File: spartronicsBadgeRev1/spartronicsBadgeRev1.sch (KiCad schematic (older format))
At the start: 54 parts, among them U1 ATmega328PB-AU

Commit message: Checkpoint before doing routing, in case of error
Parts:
- J_Debug1: footprint Connector_PinSocket_2.54mm:PinSocket_2x03_P2.54mm_Horizontal -> Connector_PinHeader_2.54mm:PinHeader_2x03_P2.54mm_Vertical
- J_ExtPwr1: footprint Connector_PinSocket_2.54mm:PinSocket_1x02_P2.54mm_Horizontal -> Connector_PinHeader_2.54mm:PinHeader_1x02_P2.54mm_Vertical
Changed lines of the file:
@@
 EESchema Schematic File Version 4
 LIBS:spartronicsBadgeRev1-cache
-EELAYER 26 0
+EELAYER 30 0
 EELAYER END
 $Descr A4 11693 8268
@@
 F 0 "J_ExtPwr1" V 4650 1100 50  0000 L CNN
 F 1 "Conn_01x02" V 4750 850 50  0000 L CNN
-F 2 "Connector_PinSocket_2.54mm:PinSocket_1x02_P2.54mm_Horizontal" H 4650 1000 50  0001 C CNN
+F 2 "Connector_PinHeader_2.54mm:PinHeader_1x02_P2.54mm_Vertical" H 4650 1000 50  0001 C CNN
 F 3 "~" H 4650 1000 50  0001 C CNN
 	1    4650 1000
@@
 F 0 "J_Debug1" H 4700 3467 50  0000 C CNN
 F 1 "Conn_02x03" H 4700 3376 50  0000 C CNN
-F 2 "Connector_PinSocket_2.54mm:PinSocket_2x03_P2.54mm_Horizontal" H 4650 3150 50  0001 C CNN
+F 2 "Connector_PinHeader_2.54mm:PinHeader_2x03_P2.54mm_Vertical" H 4650 3150 50  0001 C CNN
 F 3 "~" H 4650 3150 50  0001 C CNN
 	1    4650 3150

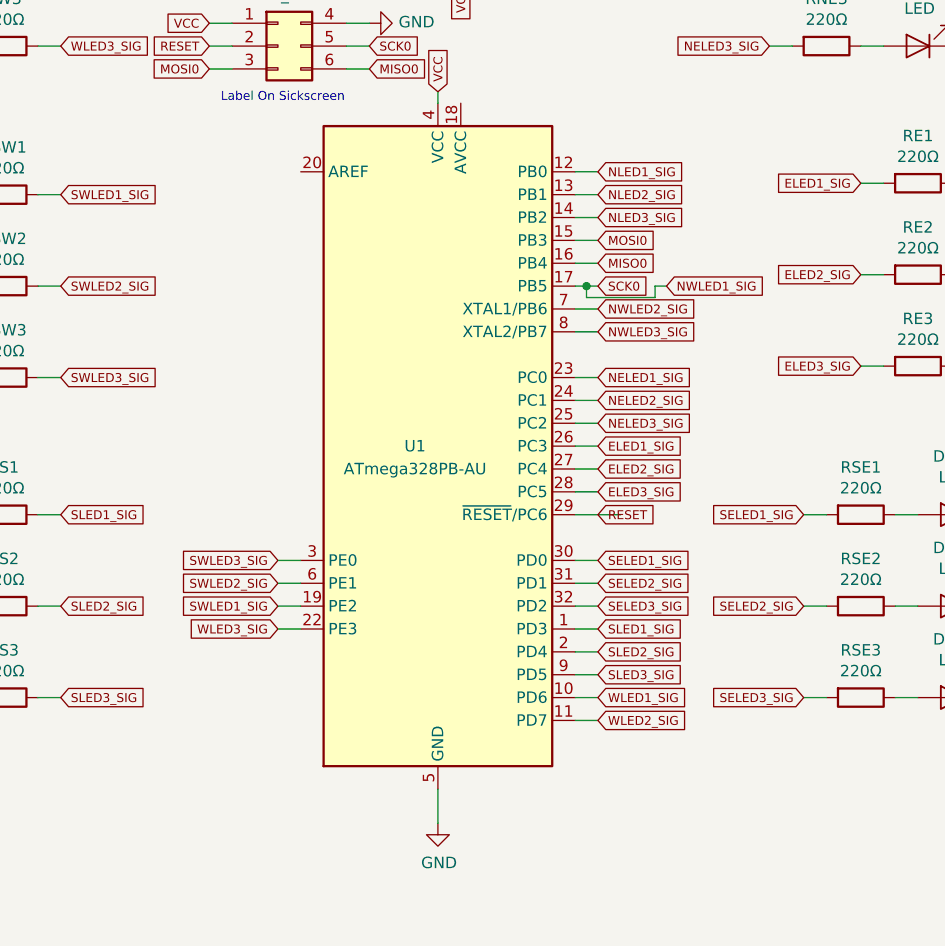
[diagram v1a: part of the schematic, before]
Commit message: Finished routing, labels on back, added ground plane. Almost ready for build
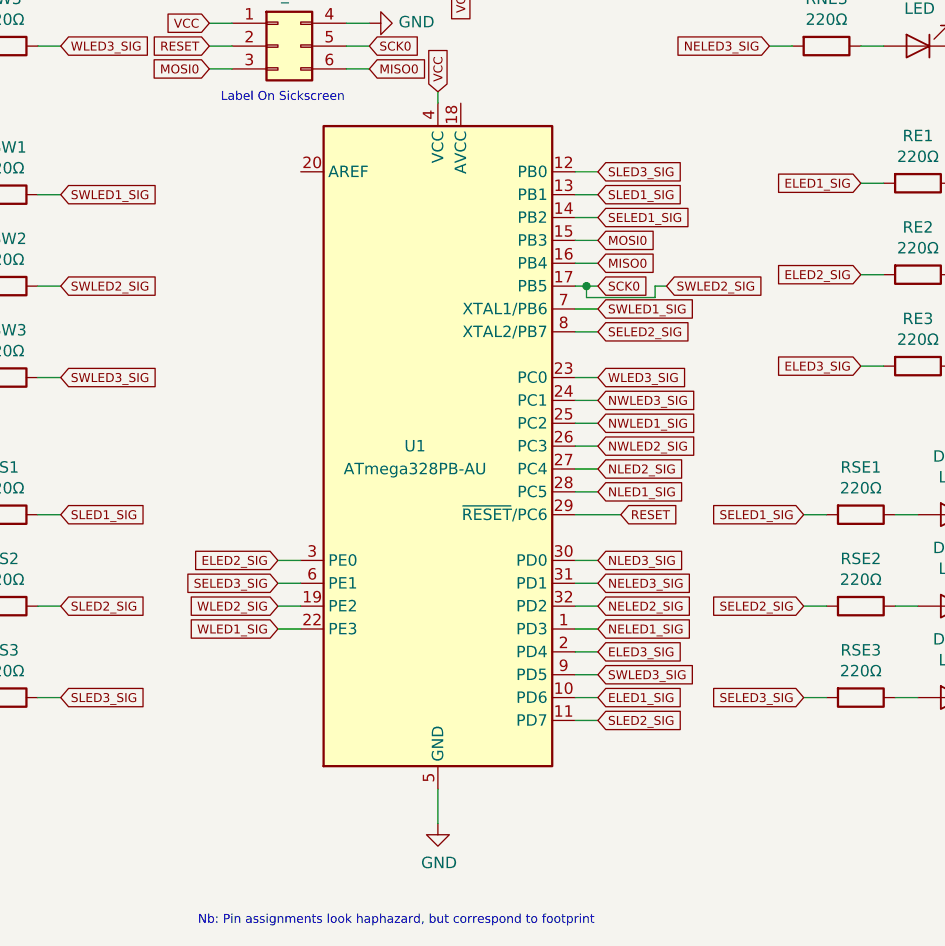
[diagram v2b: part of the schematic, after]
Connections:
- net ELED1_SIG: now also U1.10 (PD6); no longer U1.26 (PC3)
- net ELED2_SIG: now also U1.3 (PE0); no longer U1.27 (PC4)
- net ELED3_SIG: now also U1.2 (PD4); no longer U1.28 (PC5)
- net NELED1_SIG: now also U1.1 (PD3); no longer U1.23 (PC0)
- net NELED2_SIG: now also U1.32 (PD2); no longer U1.24 (PC1)
- net NELED3_SIG: now also U1.31 (PD1); no longer U1.25 (PC2)
- net NLED1_SIG: now also U1.28 (PC5); no longer U1.12 (PB0)
- net NLED2_SIG: now also U1.27 (PC4); no longer U1.13 (PB1)
- net NLED3_SIG: now also U1.30 (PD0); no longer U1.14 (PB2)
- net NWLED1_SIG: now also U1.25 (PC2); no longer J_Debug1.5 (Pin_5), U1.17 (PB5)
- net NWLED2_SIG: now also U1.26 (PC3); no longer U1.7 (XTAL1/PB6)
- net NWLED3_SIG: now also U1.24 (PC1); no longer U1.8 (XTAL2/PB7)
- net SELED1_SIG: now also U1.14 (PB2); no longer U1.30 (PD0)
- net SELED2_SIG: now also U1.8 (XTAL2/PB7); no longer U1.31 (PD1)
- net SELED3_SIG: now also U1.6 (PE1); no longer U1.32 (PD2)
- net SLED1_SIG: now also U1.13 (PB1); no longer U1.1 (PD3)
- net SLED2_SIG: now also U1.11 (PD7); no longer U1.2 (PD4)
- net SLED3_SIG: now also U1.12 (PB0); no longer U1.9 (PD5)
- net SWLED1_SIG: now also U1.7 (XTAL1/PB6); no longer U1.19 (PE2)
- net SWLED3_SIG: now also U1.9 (PD5); no longer U1.3 (PE0)
- net WLED1_SIG: now also U1.22 (PE3); no longer U1.10 (PD6)
- net WLED2_SIG: now also U1.19 (PE2); no longer U1.11 (PD7)
- net WLED3_SIG: now also U1.23 (PC0); no longer U1.22 (PE3)
- net SWLED2_SIG renamed SCK0
- net SCK0: now also J_Debug1.5 (Pin_5), U1.17 (PB5); no longer U1.6 (PE1)
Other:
- note added: "Nb: Pin assignments look haphazard, but correspond to footprint\n"
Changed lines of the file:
@@
 	1    0    0    -1
 $EndComp
-Text GLabel 6050 5200 2    39   Input ~ 0
+Text GLabel 6150 5200 2    39   Input ~ 0
 RESET
 Wire Wire Line
@@
 Text Notes 4100 1850 0    39   ~ 0
 Later Revisions add reverse \nprotection(shotkeyy) diode here?
+Text GLabel 6050 5100 2    39   Input ~ 0
+NLED1_SIG
+Text GLabel 6050 5000 2    39   Input ~ 0
+NLED2_SIG
+Text GLabel 6050 5400 2    39   Input ~ 0
+NLED3_SIG
+Wire Wire Line
+	5950 3700 6050 3700
+Wire Wire Line
+	5950 3800 6050 3800
+Wire Wire Line
+	5950 3900 6050 3900
+Text GLabel 6050 5700 2    39   Input ~ 0
+NELED1_SIG
+Text GLabel 6050 5600 2    39   Input ~ 0
+NELED2_SIG
+Text GLabel 6050 5500 2    39   Input ~ 0
+NELED3_SIG
+Text GLabel 6050 6000 2    39   Input ~ 0
+ELED1_SIG
+Text GLabel 4650 5400 0    39   Input ~ 0
+ELED2_SIG
+Text GLabel 6050 5800 2    39   Input ~ 0
+ELED3_SIG
+Text GLabel 6050 3900 2    39   Input ~ 0
+SELED1_SIG
+Text GLabel 6050 4400 2    39   Input ~ 0
+SELED2_SIG
+Text GLabel 4650 5500 0    39   Input ~ 0
+SELED3_SIG
+Text GLabel 6050 3800 2    39   Input ~ 0
+SLED1_SIG
+Text GLabel 6050 6100 2    39   Input ~ 0
+SLED2_SIG
 Text GLabel 6050 3700 2    39   Input ~ 0
-NLED1_SIG
-Text GLabel 6050 3800 2    39   Input ~ 0
-NLED2_SIG
-Text GLabel 6050 3900 2    39   Input ~ 0
-NLED3_SIG
-Wire Wire Line
-	5950 3700 6050 3700
-Wire Wire Line
-	5950 3800 6050 3800
-Wire Wire Line
-	5950 3900 6050 3900
-Text GLabel 6050 4600 2    39   Input ~ 0
-NELED1_SIG
-Text GLabel 6050 4700 2    39   Input ~ 0
-NELED2_SIG
-Text GLabel 6050 4800 2    39   Input ~ 0
-NELED3_SIG
-Text GLabel 6050 4900 2    39   Input ~ 0
-ELED1_SIG
-Text GLabel 6050 5000 2    39   Input ~ 0
-ELED2_SIG
-Text GLabel 6050 5100 2    39   Input ~ 0
-ELED3_SIG
-Text GLabel 6050 5400 2    39   Input ~ 0
-SELED1_SIG
-Text GLabel 6050 5500 2    39   Input ~ 0
-SELED2_SIG
-Text GLabel 6050 5600 2    39   Input ~ 0
-SELED3_SIG
-Text GLabel 6050 5700 2    39   Input ~ 0
-SLED1_SIG
-Text GLabel 6050 5800 2    39   Input ~ 0
-SLED2_SIG
+SLED3_SIG
+Text GLabel 6050 4300 2    39   Input ~ 0
+SWLED1_SIG
+Text GLabel 6350 4200 2    39   Input ~ 0
+SWLED2_SIG
 Text GLabel 6050 5900 2    39   Input ~ 0
-SLED3_SIG
-Text GLabel 4650 5600 0    39   Input ~ 0
-SWLED1_SIG
-Text GLabel 4650 5500 0    39   Input ~ 0
-SWLED2_SIG
-Text GLabel 4650 5400 0    39   Input ~ 0
 SWLED3_SIG
 $Comp
@@
 	0    1    1    0
 $EndComp
-Text GLabel 6050 6000 2    39   Input ~ 0
+Text GLabel 4650 5700 0    39   Input ~ 0
 WLED1_SIG
-Text GLabel 6050 6100 2    39   Input ~ 0
+Text GLabel 4650 5600 0    39   Input ~ 0
 WLED2_SIG
-Text GLabel 4650 5700 0    39   Input ~ 0
+Text GLabel 6050 4600 2    39   Input ~ 0
 WLED3_SIG
 Wire Wire Line
@@
 Wire Wire Line
 	6050 4600 5950 4600
-Text GLabel 6350 4200 2    39   Input ~ 0
+Text GLabel 6050 4800 2    39   Input ~ 0
 NWLED1_SIG
-Text GLabel 6050 4300 2    39   Input ~ 0
+Text GLabel 6050 4900 2    39   Input ~ 0
 NWLED2_SIG
-Text GLabel 6050 4400 2    39   Input ~ 0
+Text GLabel 6050 4700 2    39   Input ~ 0
 NWLED3_SIG
 Wire Wire Line
@@
 Wire Wire Line
 	5150 1000 5050 1000
+Text Notes 4300 7000 0    39   ~ 0
+Nb: Pin assignments look haphazard, but correspond to footprint\n
 $EndSCHEMATC

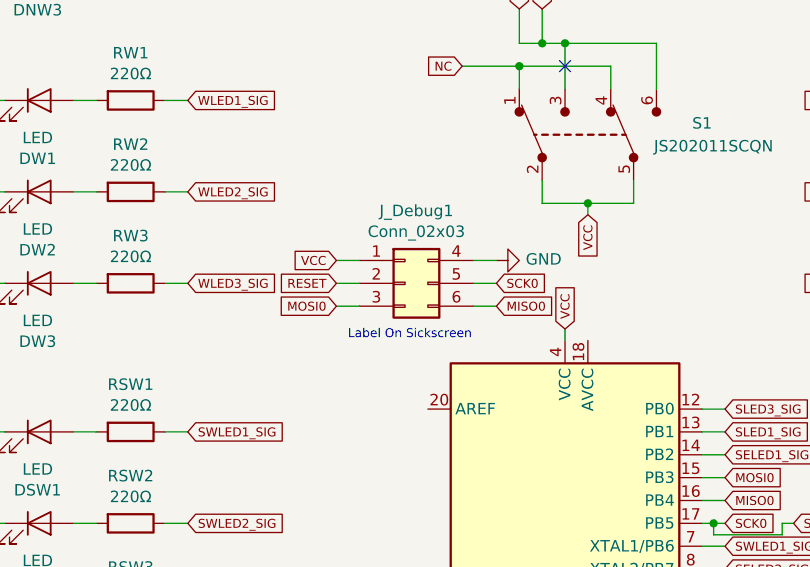
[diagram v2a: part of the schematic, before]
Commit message: :dizzy: Re-assigning footprint to Diodes + Debug connector (Had to re-assign some pins) (Full 3D render now!)
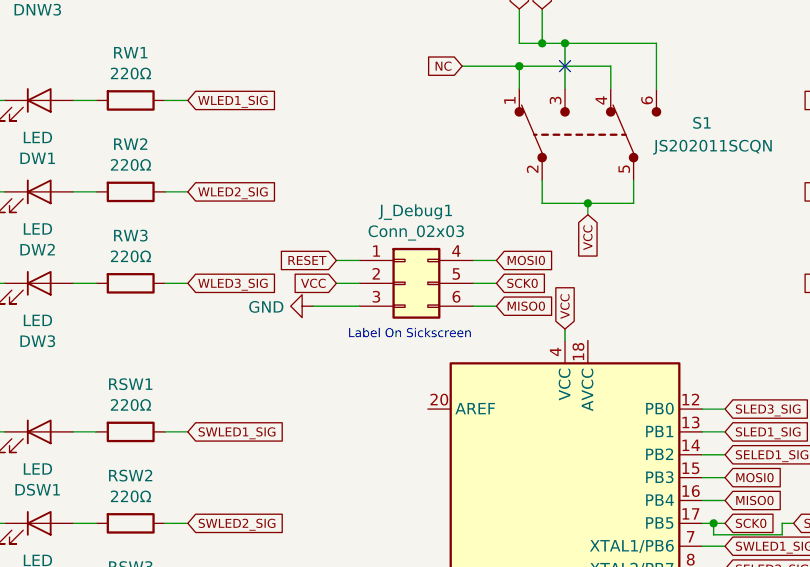
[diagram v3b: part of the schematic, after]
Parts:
- DE1, DE2, DE3, DN1, DN2, DN3, DNE1, DNE2, DNE3, DNW1, DNW2, DNW3, DS1, DS2, DS3, DSE1, DSE2, DSE3, DSW1, DSW2, DSW3, DW1, DW2, DW3: footprint Diode_SMD:D_0603_1608Metric_Pad1.05x0.95mm_HandSolder -> LED_SMD:LED_0603_1608Metric_Pad1.05x0.95mm_HandSolder
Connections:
- net GND: now also J_Debug1.3 (Pin_3); no longer J_Debug1.4 (Pin_4)
- net MOSI0: now also J_Debug1.4 (Pin_4); no longer J_Debug1.3 (Pin_3)
- net RESET: now also J_Debug1.1 (Pin_1); no longer J_Debug1.2 (Pin_2)
- net VCC: now also J_Debug1.2 (Pin_2); no longer J_Debug1.1 (Pin_1)
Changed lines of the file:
@@
 F 0 "DN1" H 7643 645 50  0000 C CNN
 F 1 "LED" H 7643 736 50  0000 C CNN
-F 2 "Diode_SMD:D_0603_1608Metric_Pad1.05x0.95mm_HandSolder" H 7650 900 50  0001 C CNN
+F 2 "LED_SMD:LED_0603_1608Metric_Pad1.05x0.95mm_HandSolder" H 7650 900 50  0001 C CNN
 F 3 "~" H 7650 900 50  0001 C CNN
 	1    7650 900
@@
 F 0 "DN2" H 7643 1045 50  0000 C CNN
 F 1 "LED" H 7643 1136 50  0000 C CNN
-F 2 "Diode_SMD:D_0603_1608Metric_Pad1.05x0.95mm_HandSolder" H 7650 1300 50  0001 C CNN
+F 2 "LED_SMD:LED_0603_1608Metric_Pad1.05x0.95mm_HandSolder" H 7650 1300 50  0001 C CNN
 F 3 "~" H 7650 1300 50  0001 C CNN
 	1    7650 1300
@@
 F 0 "DN3" H 7643 1445 50  0000 C CNN
 F 1 "LED" H 7643 1536 50  0000 C CNN
-F 2 "Diode_SMD:D_0603_1608Metric_Pad1.05x0.95mm_HandSolder" H 7650 1700 50  0001 C CNN
+F 2 "LED_SMD:LED_0603_1608Metric_Pad1.05x0.95mm_HandSolder" H 7650 1700 50  0001 C CNN
 F 3 "~" H 7650 1700 50  0001 C CNN
 	1    7650 1700
@@
 F 0 "DNE1" H 7443 2095 50  0000 C CNN
 F 1 "LED" H 7443 2186 50  0000 C CNN
-F 2 "Diode_SMD:D_0603_1608Metric_Pad1.05x0.95mm_HandSolder" H 7450 2350 50  0001 C CNN
+F 2 "LED_SMD:LED_0603_1608Metric_Pad1.05x0.95mm_HandSolder" H 7450 2350 50  0001 C CNN
 F 3 "~" H 7450 2350 50  0001 C CNN
 	1    7450 2350
@@
 F 0 "DNE2" H 7443 2495 50  0000 C CNN
 F 1 "LED" H 7443 2586 50  0000 C CNN
-F 2 "Diode_SMD:D_0603_1608Metric_Pad1.05x0.95mm_HandSolder" H 7450 2750 50  0001 C CNN
+F 2 "LED_SMD:LED_0603_1608Metric_Pad1.05x0.95mm_HandSolder" H 7450 2750 50  0001 C CNN
 F 3 "~" H 7450 2750 50  0001 C CNN
 	1    7450 2750
@@
 F 0 "DNE3" H 7443 2895 50  0000 C CNN
 F 1 "LED" H 7443 2986 50  0000 C CNN
-F 2 "Diode_SMD:D_0603_1608Metric_Pad1.05x0.95mm_HandSolder" H 7450 3150 50  0001 C CNN
+F 2 "LED_SMD:LED_0603_1608Metric_Pad1.05x0.95mm_HandSolder" H 7450 3150 50  0001 C CNN
 F 3 "~" H 7450 3150 50  0001 C CNN
 	1    7450 3150
@@
 F 0 "DE1" H 7843 3495 50  0000 C CNN
 F 1 "LED" H 7843 3586 50  0000 C CNN
-F 2 "Diode_SMD:D_0603_1608Metric_Pad1.05x0.95mm_HandSolder" H 7850 3750 50  0001 C CNN
+F 2 "LED_SMD:LED_0603_1608Metric_Pad1.05x0.95mm_HandSolder" H 7850 3750 50  0001 C CNN
 F 3 "~" H 7850 3750 50  0001 C CNN
 	1    7850 3750
@@
 F 0 "DE2" H 7843 3895 50  0000 C CNN
 F 1 "LED" H 7843 3986 50  0000 C CNN
-F 2 "Diode_SMD:D_0603_1608Metric_Pad1.05x0.95mm_HandSolder" H 7850 4150 50  0001 C CNN
+F 2 "LED_SMD:LED_0603_1608Metric_Pad1.05x0.95mm_HandSolder" H 7850 4150 50  0001 C CNN
 F 3 "~" H 7850 4150 50  0001 C CNN
 	1    7850 4150
@@
 F 0 "DE3" H 7843 4295 50  0000 C CNN
 F 1 "LED" H 7843 4386 50  0000 C CNN
-F 2 "Diode_SMD:D_0603_1608Metric_Pad1.05x0.95mm_HandSolder" H 7850 4550 50  0001 C CNN
+F 2 "LED_SMD:LED_0603_1608Metric_Pad1.05x0.95mm_HandSolder" H 7850 4550 50  0001 C CNN
 F 3 "~" H 7850 4550 50  0001 C CNN
 	1    7850 4550
@@
 F 0 "DSE1" H 7593 4945 50  0000 C CNN
 F 1 "LED" H 7593 5036 50  0000 C CNN
-F 2 "Diode_SMD:D_0603_1608Metric_Pad1.05x0.95mm_HandSolder" H 7600 5200 50  0001 C CNN
+F 2 "LED_SMD:LED_0603_1608Metric_Pad1.05x0.95mm_HandSolder" H 7600 5200 50  0001 C CNN
 F 3 "~" H 7600 5200 50  0001 C CNN
 	1    7600 5200
@@
 F 0 "DSE2" H 7593 5345 50  0000 C CNN
 F 1 "LED" H 7593 5436 50  0000 C CNN
-F 2 "Diode_SMD:D_0603_1608Metric_Pad1.05x0.95mm_HandSolder" H 7600 5600 50  0001 C CNN
+F 2 "LED_SMD:LED_0603_1608Metric_Pad1.05x0.95mm_HandSolder" H 7600 5600 50  0001 C CNN
 F 3 "~" H 7600 5600 50  0001 C CNN
 	1    7600 5600
@@
 F 0 "DSE3" H 7593 5745 50  0000 C CNN
 F 1 "LED" H 7593 5836 50  0000 C CNN
-F 2 "Diode_SMD:D_0603_1608Metric_Pad1.05x0.95mm_HandSolder" H 7600 6000 50  0001 C CNN
+F 2 "LED_SMD:LED_0603_1608Metric_Pad1.05x0.95mm_HandSolder" H 7600 6000 50  0001 C CNN
 F 3 "~" H 7600 6000 50  0001 C CNN
 	1    7600 6000
@@
 F 0 "DNW3" H 3043 1445 50  0000 C CNN
 F 1 "LED" H 3043 1536 50  0000 C CNN
-F 2 "Diode_SMD:D_0603_1608Metric_Pad1.05x0.95mm_HandSolder" H 3050 1700 50  0001 C CNN
+F 2 "LED_SMD:LED_0603_1608Metric_Pad1.05x0.95mm_HandSolder" H 3050 1700 50  0001 C CNN
 F 3 "~" H 3050 1700 50  0001 C CNN
 	1    3050 1700
@@
 F 0 "DNW2" H 3043 1045 50  0000 C CNN
 F 1 "LED" H 3043 1136 50  0000 C CNN
-F 2 "Diode_SMD:D_0603_1608Metric_Pad1.05x0.95mm_HandSolder" H 3050 1300 50  0001 C CNN
+F 2 "LED_SMD:LED_0603_1608Metric_Pad1.05x0.95mm_HandSolder" H 3050 1300 50  0001 C CNN
 F 3 "~" H 3050 1300 50  0001 C CNN
 	1    3050 1300
@@
 F 0 "DNW1" H 3043 645 50  0000 C CNN
 F 1 "LED" H 3043 736 50  0000 C CNN
-F 2 "Diode_SMD:D_0603_1608Metric_Pad1.05x0.95mm_HandSolder" H 3050 900 50  0001 C CNN
+F 2 "LED_SMD:LED_0603_1608Metric_Pad1.05x0.95mm_HandSolder" H 3050 900 50  0001 C CNN
 F 3 "~" H 3050 900 50  0001 C CNN
 	1    3050 900
@@
 F 0 "DW3" H 3043 2895 50  0000 C CNN
 F 1 "LED" H 3043 2986 50  0000 C CNN
-F 2 "Diode_SMD:D_0603_1608Metric_Pad1.05x0.95mm_HandSolder" H 3050 3150 50  0001 C CNN
+F 2 "LED_SMD:LED_0603_1608Metric_Pad1.05x0.95mm_HandSolder" H 3050 3150 50  0001 C CNN
 F 3 "~" H 3050 3150 50  0001 C CNN
 	1    3050 3150
@@
 F 0 "DW2" H 3043 2495 50  0000 C CNN
 F 1 "LED" H 3043 2586 50  0000 C CNN
-F 2 "Diode_SMD:D_0603_1608Metric_Pad1.05x0.95mm_HandSolder" H 3050 2750 50  0001 C CNN
+F 2 "LED_SMD:LED_0603_1608Metric_Pad1.05x0.95mm_HandSolder" H 3050 2750 50  0001 C CNN
 F 3 "~" H 3050 2750 50  0001 C CNN
 	1    3050 2750
@@
 F 0 "DW1" H 3043 2095 50  0000 C CNN
 F 1 "LED" H 3043 2186 50  0000 C CNN
-F 2 "Diode_SMD:D_0603_1608Metric_Pad1.05x0.95mm_HandSolder" H 3050 2350 50  0001 C CNN
+F 2 "LED_SMD:LED_0603_1608Metric_Pad1.05x0.95mm_HandSolder" H 3050 2350 50  0001 C CNN
 F 3 "~" H 3050 2350 50  0001 C CNN
 	1    3050 2350
@@
 F 0 "DSW3" H 3043 4345 50  0000 C CNN
 F 1 "LED" H 3043 4436 50  0000 C CNN
-F 2 "Diode_SMD:D_0603_1608Metric_Pad1.05x0.95mm_HandSolder" H 3050 4600 50  0001 C CNN
+F 2 "LED_SMD:LED_0603_1608Metric_Pad1.05x0.95mm_HandSolder" H 3050 4600 50  0001 C CNN
 F 3 "~" H 3050 4600 50  0001 C CNN
 	1    3050 4600
@@
 F 0 "DSW2" H 3043 3945 50  0000 C CNN
 F 1 "LED" H 3043 4036 50  0000 C CNN
-F 2 "Diode_SMD:D_0603_1608Metric_Pad1.05x0.95mm_HandSolder" H 3050 4200 50  0001 C CNN
+F 2 "LED_SMD:LED_0603_1608Metric_Pad1.05x0.95mm_HandSolder" H 3050 4200 50  0001 C CNN
 F 3 "~" H 3050 4200 50  0001 C CNN
 	1    3050 4200
@@
 F 0 "DSW1" H 3043 3545 50  0000 C CNN
 F 1 "LED" H 3043 3636 50  0000 C CNN
-F 2 "Diode_SMD:D_0603_1608Metric_Pad1.05x0.95mm_HandSolder" H 3050 3800 50  0001 C CNN
+F 2 "LED_SMD:LED_0603_1608Metric_Pad1.05x0.95mm_HandSolder" H 3050 3800 50  0001 C CNN
 F 3 "~" H 3050 3800 50  0001 C CNN
 	1    3050 3800
@@
 F 0 "DS3" H 3043 5745 50  0000 C CNN
 F 1 "LED" H 3043 5836 50  0000 C CNN
-F 2 "Diode_SMD:D_0603_1608Metric_Pad1.05x0.95mm_HandSolder" H 3050 6000 50  0001 C CNN
+F 2 "LED_SMD:LED_0603_1608Metric_Pad1.05x0.95mm_HandSolder" H 3050 6000 50  0001 C CNN
 F 3 "~" H 3050 6000 50  0001 C CNN
 	1    3050 6000
@@
 F 0 "DS2" H 3043 5345 50  0000 C CNN
 F 1 "LED" H 3043 5436 50  0000 C CNN
-F 2 "Diode_SMD:D_0603_1608Metric_Pad1.05x0.95mm_HandSolder" H 3050 5600 50  0001 C CNN
+F 2 "LED_SMD:LED_0603_1608Metric_Pad1.05x0.95mm_HandSolder" H 3050 5600 50  0001 C CNN
 F 3 "~" H 3050 5600 50  0001 C CNN
 	1    3050 5600
@@
 F 0 "DS1" H 3043 4945 50  0000 C CNN
 F 1 "LED" H 3043 5036 50  0000 C CNN
-F 2 "Diode_SMD:D_0603_1608Metric_Pad1.05x0.95mm_HandSolder" H 3050 5200 50  0001 C CNN
+F 2 "LED_SMD:LED_0603_1608Metric_Pad1.05x0.95mm_HandSolder" H 3050 5200 50  0001 C CNN
 F 3 "~" H 3050 5200 50  0001 C CNN
 	1    3050 5200
@@
 Wire Wire Line
 	5950 5200 6150 5200
-Text GLabel 4350 3150 0    39   Input ~ 0
+Text GLabel 4350 3050 0    39   Input ~ 0
 RESET
 Wire Wire Line
@@
 Wire Wire Line
 	4950 3150 5050 3150
-Text GLabel 4350 3250 0    39   Input ~ 0
+Text GLabel 5050 3050 2    39   Input ~ 0
 MOSI0
 Text GLabel 5050 3250 2    39   Input ~ 0
@@
 Wire Wire Line
 	4950 3250 5050 3250
-Wire Wire Line
-	4450 3250 4350 3250
 $Comp
 L power:GND #PWR0104
 U 1 1 5E1237AE
-P 5050 3050
-F 0 "#PWR0104" H 5050 2800 50  0001 C CNN
-F 1 "GND" V 5055 2922 50  0000 R CNN
-F 2 "" H 5050 3050 50  0001 C CNN
-F 3 "" H 5050 3050 50  0001 C CNN
-	1    5050 3050
-	0    -1   -1   0
-$EndComp
-Wire Wire Line
-	4950 3050 5050 3050
+P 4250 3250
+F 0 "#PWR0104" H 4250 3000 50  0001 C CNN
+F 1 "GND" V 4255 3122 50  0000 R CNN
+F 2 "" H 4250 3250 50  0001 C CNN
+F 3 "" H 4250 3250 50  0001 C CNN
+	1    4250 3250
+	0    1    1    0
+$EndComp
 Wire Wire Line
 	5250 2800 5450 2800
@@
 Text Notes 6000 1100 0    39   ~ 0
 Ground Plane\n
-Text GLabel 4350 3050 0    39   Input ~ 0
+Text GLabel 4350 3150 0    39   Input ~ 0
 VCC
 Wire Wire Line
@@
 Text Notes 4300 7000 0    39   ~ 0
 Nb: Pin assignments look haphazard, but correspond to footprint\n
+Wire Wire Line
+	4950 3050 5050 3050
+Wire Wire Line
+	4250 3250 4450 3250
 $EndSCHEMATC
